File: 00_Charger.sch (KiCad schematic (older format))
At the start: 42 parts, among them J401 TB001-500-02BE CUI_Devices, Q401 NTK3043N, Q402 FDD4685-F085, U401 MAX1873TEEE, U402 PC827

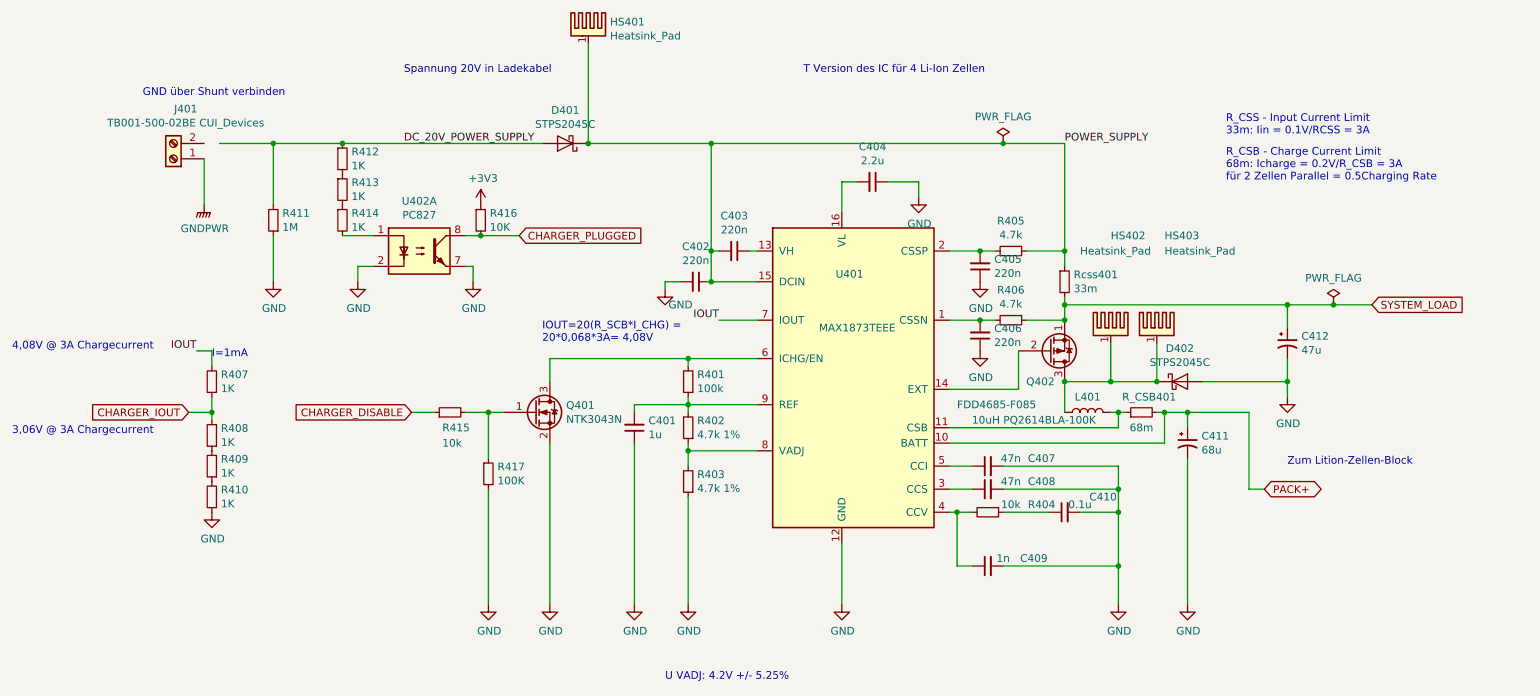
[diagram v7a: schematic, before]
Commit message: PCB angefangen: Charger geplaced
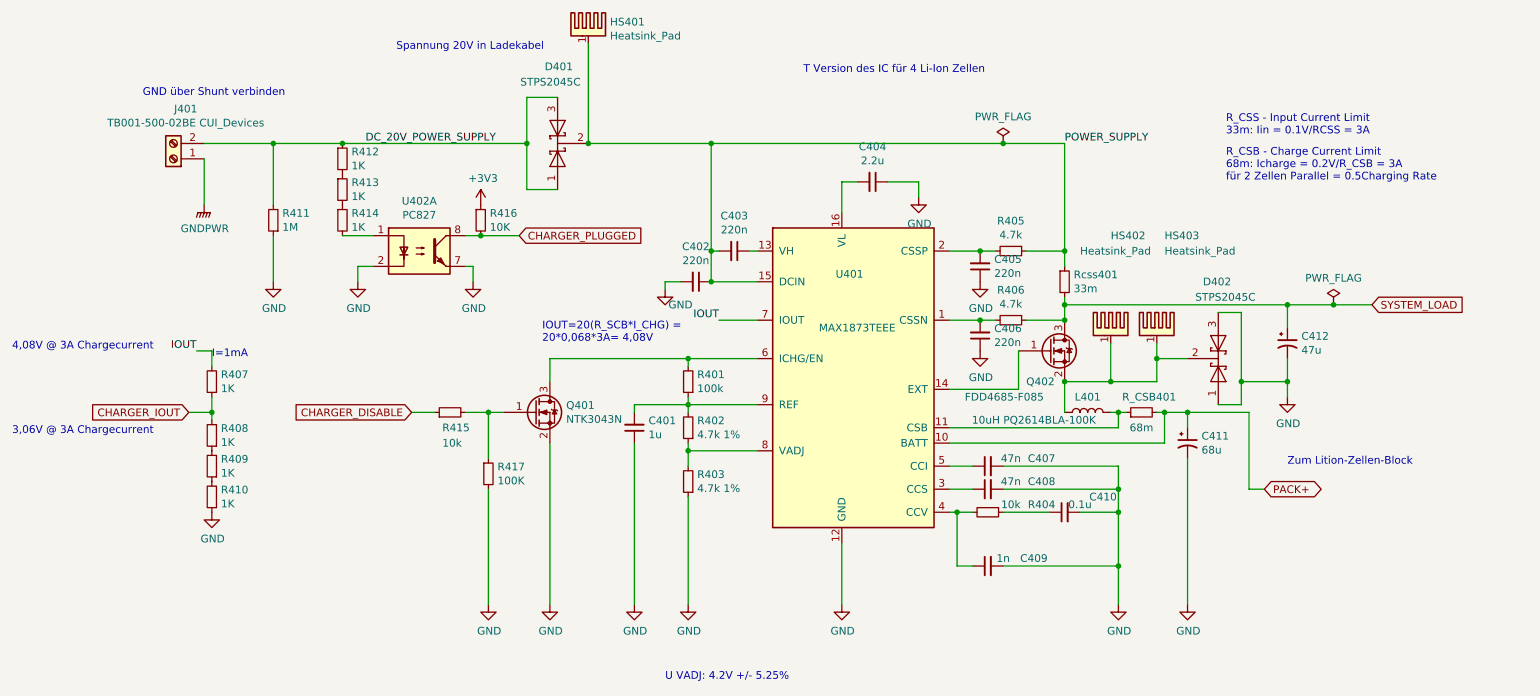
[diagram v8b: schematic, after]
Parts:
- removed D401, D402: STPS2045C, Package_TO_SOT_SMD:TO-263-2, symbol Device:D_Schottky
- removed Q402: FDD4685-F085, Package_TO_SOT_SMD:TO-263-2, symbol Device:Q_PMOS_SGD
- added D401, D402: STPS2045C, Package_TO_SOT_SMD:TO-263-2, symbol Device:D_Schottky_x2_KCom_AKA
- added Q402: FDD4685-F085, Package_TO_SOT_SMD:TO-263-2, symbol Device:Q_NMOS_GSD
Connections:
- net DC_20V_POWER_SUPPLY: now also J401.2 (Pin_2), D401.1 (A), D401.3 (A)
- net GND: now also D402.1 (A), D402.3 (A)
- net POWER_SUPPLY: now also D401.2 (K)
- net SYSTEM_LOAD: now also Q402.3 (D)
- net at U401.14 (EXT): now also Q402.1 (G)
- net at HS402.1, HS403.1, L401.1: now also D402.2 (K), Q402.2 (S)
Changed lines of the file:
@@
-$EndComp
-$Comp
-L Device:Q_PMOS_SGD Q402
-U 1 1 5E740451
-P 7750 3550
-F 0 "Q402" H 7600 3750 50  0000 L CNN
-F 1 "FDD4685-F085" H 7150 3900 50  0000 L CNN
-F 2 "Package_TO_SOT_SMD:TO-263-2" H 7950 3650 50  0001 C CNN
-F 3 "~" H 7750 3550 50  0001 C CNN
-	1    7750 3550
-	1    0    0    1
 $EndComp
 $Comp
@@
 Text GLabel 2150 3950 0    50   Input ~ 0
 CHARGER_IOUT
-$Comp
-L Device:D_Schottky D401
-U 1 1 5E74F959
-P 4600 2200
-F 0 "D401" H 4600 1984 50  0000 C CNN
-F 1 "STPS2045C" H 4600 2075 50  0000 C CNN
-F 2 "Package_TO_SOT_SMD:TO-263-2" H 4600 2200 50  0001 C CNN
-F 3 "~" H 4600 2200 50  0001 C CNN
-	1    4600 2200
-	-1   0    0    1
-$EndComp
 $Comp
 L Device:R_Small R405
@@
 	1    0    0    -1
 $EndComp
-$Comp
-L Device:D_Schottky D402
-U 1 1 5E838BD2
-P 8600 3750
-F 0 "D402" H 8600 3966 50  0000 C CNN
-F 1 "STPS2045C" H 8600 3875 50  0000 C CNN
-F 2 "Package_TO_SOT_SMD:TO-263-2" H 8600 3750 50  0001 C CNN
-F 3 "~" H 8600 3750 50  0001 C CNN
-	1    8600 3750
-	1    0    0    -1
-$EndComp
-Connection ~ 7850 3350
 Wire Wire Line
 	7550 3550 7550 3800
 Wire Wire Line
 	7850 3750 7850 3950
-Connection ~ 7850 3750
 Wire Wire Line
 	8200 3950 8200 4050
@@
 Wire Wire Line
 	9300 3750 9300 3850
-Wire Wire Line
-	8750 3750 9300 3750
 Connection ~ 9300 3750
 Wire Wire Line
@@
 Text GLabel 9150 4450 2    50   BiDi ~ 0
 PACK+
-Text Notes 3550 1750 0    50   ~ 0
+Text Notes 3500 1600 0    50   ~ 0
 Spannung 20V in Ladekabel
 $Comp
@@
 Text Notes 1850 1900 0    50   ~ 0
 GND über Shunt verbinden
-Text Label 3550 2200 0    50   ~ 0
+Text Label 3300 2200 0    50   ~ 0
 DC_20V_POWER_SUPPLY
 $Comp
@@
 Wire Wire Line
 	3250 3000 3250 3100
-Wire Wire Line
-	2350 2200 2700 2200
 $Comp
 L Device:R_Small R412
@@
 Connection ~ 3150 2200
 Wire Wire Line
-	3150 2200 4450 2200
+	3150 2200 4350 2200
 $Comp
 L Device:R_Small R413
@@
 Wire Wire Line
 	4750 1550 4750 2200
-Connection ~ 4750 2200
 $Comp
 L Mechanical:Heatsink_Pad HS403
@@
 	8150 3750 8450 3750
 Wire Wire Line
-	8450 3500 8450 3750
-Connection ~ 8450 3750
+	8450 3500 8450 3600
 Wire Wire Line
 	4750 2200 5550 2200
@@
 	-1   0    0    1
 $EndComp
+Wire Wire Line
+	2250 2200 2700 2200
+$Comp
+L Device:Q_NMOS_GSD Q402
+U 1 1 5E98AB96
+P 7750 3550
+F 0 "Q402" H 7600 3350 50  0000 L CNN
+F 1 "FDD4685-F085" H 7200 3250 50  0000 L CNN
+F 2 "Package_TO_SOT_SMD:TO-263-2" H 7950 3650 50  0001 C CNN
+F 3 "https://www.mouser.de/datasheet/2/308/FDD4685_F085-D-1807000.pdf" H 7750 3550 50  0001 C CNN
+	1    7750 3550
+	1    0    0    -1
+$EndComp
+Connection ~ 7850 3750
+Connection ~ 7850 3350
+$Comp
+L Device:D_Schottky_x2_KCom_AKA D?
+U 1 1 5E990B16
+P 4550 2200
+AR Path="/5E73BAE8/5E990B16" Ref="D?"  Part="1"
+AR Path="/5E73BB4A/5E990B16" Ref="D401"  Part="1"
+F 0 "D401" V 5050 2100 50  0000 L CNN
+F 1 "STPS2045C" V 4950 2050 50  0000 L CNN
+F 2 "Package_TO_SOT_SMD:TO-263-2" H 4550 2200 50  0001 C CNN
+F 3 "https://www.mouser.de/datasheet/2/389/cd00268203-1797199.pdf" H 4550 2200 50  0001 C CNN
+	1    4550 2200
+	0    -1   -1   0
+$EndComp
+Connection ~ 4750 2200
+Wire Wire Line
+	4550 1900 4350 1900
+Wire Wire Line
+	4350 1900 4350 2200
+Wire Wire Line
+	4550 2500 4350 2500
+Wire Wire Line
+	4350 2500 4350 2200
+Connection ~ 4350 2200
+$Comp
+L Device:D_Schottky_x2_KCom_AKA D?
+U 1 1 5E99FC60
+P 8850 3600
+AR Path="/5E73BAE8/5E99FC60" Ref="D?"  Part="1"
+AR Path="/5E73BB4A/5E99FC60" Ref="D402"  Part="1"
+F 0 "D402" V 9350 3500 50  0000 L CNN
+F 1 "STPS2045C" V 9250 3450 50  0000 L CNN
+F 2 "Package_TO_SOT_SMD:TO-263-2" H 8850 3600 50  0001 C CNN
+F 3 "https://www.mouser.de/datasheet/2/389/cd00268203-1797199.pdf" H 8850 3600 50  0001 C CNN
+	1    8850 3600
+	0    1    -1   0
+$EndComp
+Wire Wire Line
+	8650 3600 8450 3600
+Connection ~ 8450 3600
+Wire Wire Line
+	8450 3600 8450 3750
+Wire Wire Line
+	8850 3300 9000 3300
+Wire Wire Line
+	9000 3300 9000 3750
+Connection ~ 9000 3750
+Wire Wire Line
+	9000 3750 9300 3750
+Wire Wire Line
+	8850 3900 9000 3900
+Wire Wire Line
+	9000 3900 9000 3750
 $EndSCHEMATC
